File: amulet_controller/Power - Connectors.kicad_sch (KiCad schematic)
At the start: 4 parts, among them J1 XT60PW-F, J2 XT60PW-M, U6 SMBJ51CD-M3/H, U7 SMBJ51CD-M3/H

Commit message: filled in fields for bom, replaced inexisting components. Need to replace LEDs
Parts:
- J1: Manufacturer (none) -> AMASS; Manufacturer Part Number (none) -> XT60PW-F; Supplier 1 (none) -> Transfer Multisort Elektronik; Supplier Part Number 1 (none) -> XT60PW-F
- J2: Manufacturer (none) -> AMASS; Manufacturer Part Number (none) -> XT60PW-M; Supplier 1 (none) -> Transfer Multisort Elektronik; Supplier Part Number 1 (none) -> XT60PW-M
- U6, U7: Manufacturer (none) -> Vishay; Manufacturer Part Number (none) -> SMBJ51CD-M3/H; Supplier 1 (none) -> Digikey; Supplier Part Number 1 (none) -> SMBJ51CD-M3/HGICT-ND
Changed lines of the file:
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@@
     (pin "1")
     (instances
-      (project "bldc_controller"
+      (project "amulet_controller"
         (path "/0650c7a8-acba-429c-9f8e-eec0baf0bc1c/fede4c36-00cc-4d3d-b71c-5243ba232202/957e9462-5e63-4479-b30f-86013896ffc2"
           (reference "#PWR024") (unit 1)
@@
       (effects (font (size 1.27 1.27)) hide)
     )
-    (property "Datasheet" "~" (at 115.57 87.63 0)
+    (property "Datasheet" "https://www.tme.eu/Document/b13629717d44ae038681dba08d18c0b6/XT60PW-M.pdf" (at 115.57 87.63 0)
+      (effects (font (size 1.27 1.27)) hide)
+    )
+    (property "Description" "Socket; DC supply; XT60; male; PIN: 2; on PCBs; THT; yellow; 30A; 500V" (at 115.57 87.63 0)
+      (effects (font (size 1.27 1.27)) hide)
+    )
+    (property "Manufacturer" "AMASS" (at 115.57 87.63 0)
+      (effects (font (size 1.27 1.27)) hide)
+    )
+    (property "Manufacturer Part Number" "XT60PW-M" (at 115.57 87.63 0)
+      (effects (font (size 1.27 1.27)) hide)
+    )
+    (property "Supplier 1" "Transfer Multisort Elektronik" (at 115.57 87.63 0)
+      (effects (font (size 1.27 1.27)) hide)
+    )
+    (property "Supplier Part Number 1" "XT60PW-M" (at 115.57 87.63 0)
       (effects (font (size 1.27 1.27)) hide)
     )
@@
     (pin "2")
     (instances
-      (project "bldc_controller"
+      (project "amulet_controller"
         (path "/0650c7a8-acba-429c-9f8e-eec0baf0bc1c/fede4c36-00cc-4d3d-b71c-5243ba232202/957e9462-5e63-4479-b30f-86013896ffc2"
           (reference "J2") (unit 1)
@@
       (effects (font (size 1.27 1.27)) hide)
     )
+    (property "Description" "Surface-Mount TRANSZORB® Transient Voltage Suppressors" (at 135.89 77.47 0)
+      (effects (font (size 1.27 1.27)) hide)
+    )
+    (property "Manufacturer" "Vishay" (at 135.89 77.47 0)
+      (effects (font (size 1.27 1.27)) hide)
+    )
+    (property "Manufacturer Part Number" "SMBJ51CD-M3/H" (at 135.89 77.47 0)
+      (effects (font (size 1.27 1.27)) hide)
+    )
+    (property "Supplier 1" "Digikey" (at 135.89 77.47 0)
+      (effects (font (size 1.27 1.27)) hide)
+    )
+    (property "Supplier Part Number 1" "SMBJ51CD-M3/HGICT-ND" (at 135.89 77.47 0)
+      (effects (font (size 1.27 1.27)) hide)
+    )
     (pin "1")
     (pin "2")
     (instances
-      (project "bldc_controller"
+      (project "amulet_controller"
         (path "/0650c7a8-acba-429c-9f8e-eec0baf0bc1c/fede4c36-00cc-4d3d-b71c-5243ba232202/957e9462-5e63-4479-b30f-86013896ffc2"
           (reference "U6") (unit 1)
@@
       (effects (font (size 1.27 1.27)) hide)
     )
+    (property "Description" "Surface-Mount TRANSZORB® Transient Voltage Suppressors" (at 158.75 77.47 0)
+      (effects (font (size 1.27 1.27)) hide)
+    )
+    (property "Manufacturer" "Vishay" (at 158.75 77.47 0)
+      (effects (font (size 1.27 1.27)) hide)
+    )
+    (property "Manufacturer Part Number" "SMBJ51CD-M3/H" (at 158.75 77.47 0)
+      (effects (font (size 1.27 1.27)) hide)
+    )
+    (property "Supplier 1" "Digikey" (at 158.75 77.47 0)
+      (effects (font (size 1.27 1.27)) hide)
+    )
+    (property "Supplier Part Number 1" "SMBJ51CD-M3/HGICT-ND" (at 158.75 77.47 0)
+      (effects (font (size 1.27 1.27)) hide)
+    )
     (pin "1")
     (pin "2")
     (instances
-      (project "bldc_controller"
+      (project "amulet_controller"
         (path "/0650c7a8-acba-429c-9f8e-eec0baf0bc1c/fede4c36-00cc-4d3d-b71c-5243ba232202/957e9462-5e63-4479-b30f-86013896ffc2"
           (reference "U7") (unit 1)
@@
       (effects (font (size 1.27 1.27)) hide)
     )
-    (property "Datasheet" "~" (at 115.57 78.74 0)
+    (property "Datasheet" "https://www.tme.eu/Document/1191bc2fa3aee3c446e5a895fd8f7983/XT60PW-F.pdf" (at 115.57 78.74 0)
+      (effects (font (size 1.27 1.27)) hide)
+    )
+    (property "Description" "Socket; DC supply; XT60; female; PIN: 2; on PCBs; THT; yellow; 30A" (at 115.57 78.74 0)
+      (effects (font (size 1.27 1.27)) hide)
+    )
+    (property "Manufacturer" "AMASS" (at 115.57 78.74 0)
+      (effects (font (size 1.27 1.27)) hide)
+    )
+    (property "Manufacturer Part Number" "XT60PW-F" (at 115.57 78.74 0)
+      (effects (font (size 1.27 1.27)) hide)
+    )
+    (property "Supplier 1" "Transfer Multisort Elektronik" (at 115.57 78.74 0)
+      (effects (font (size 1.27 1.27)) hide)
+    )
+    (property "Supplier Part Number 1" "XT60PW-F" (at 115.57 78.74 0)
       (effects (font (size 1.27 1.27)) hide)
     )
@@
     (pin "2")
     (instances
-      (project "bldc_controller"
+      (project "amulet_controller"
         (path "/0650c7a8-acba-429c-9f8e-eec0baf0bc1c/fede4c36-00cc-4d3d-b71c-5243ba232202/957e9462-5e63-4479-b30f-86013896ffc2"
           (reference "J1") (unit 1)

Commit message: added test points
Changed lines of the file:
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@@
     (effects (font (face "Arial") (size 1.27 1.27) (color 0 0 0 1)) (justify left top))
   )
-  (text_box "Power Connectors, TVS diodes and electrolytic bulk capacitors"
+  (text_box "Power Connectors, TVS Diodes"
     (at 80.01 124.46 0) (size 134.62 9.525)
     (stroke (width -0.0001) (type default))

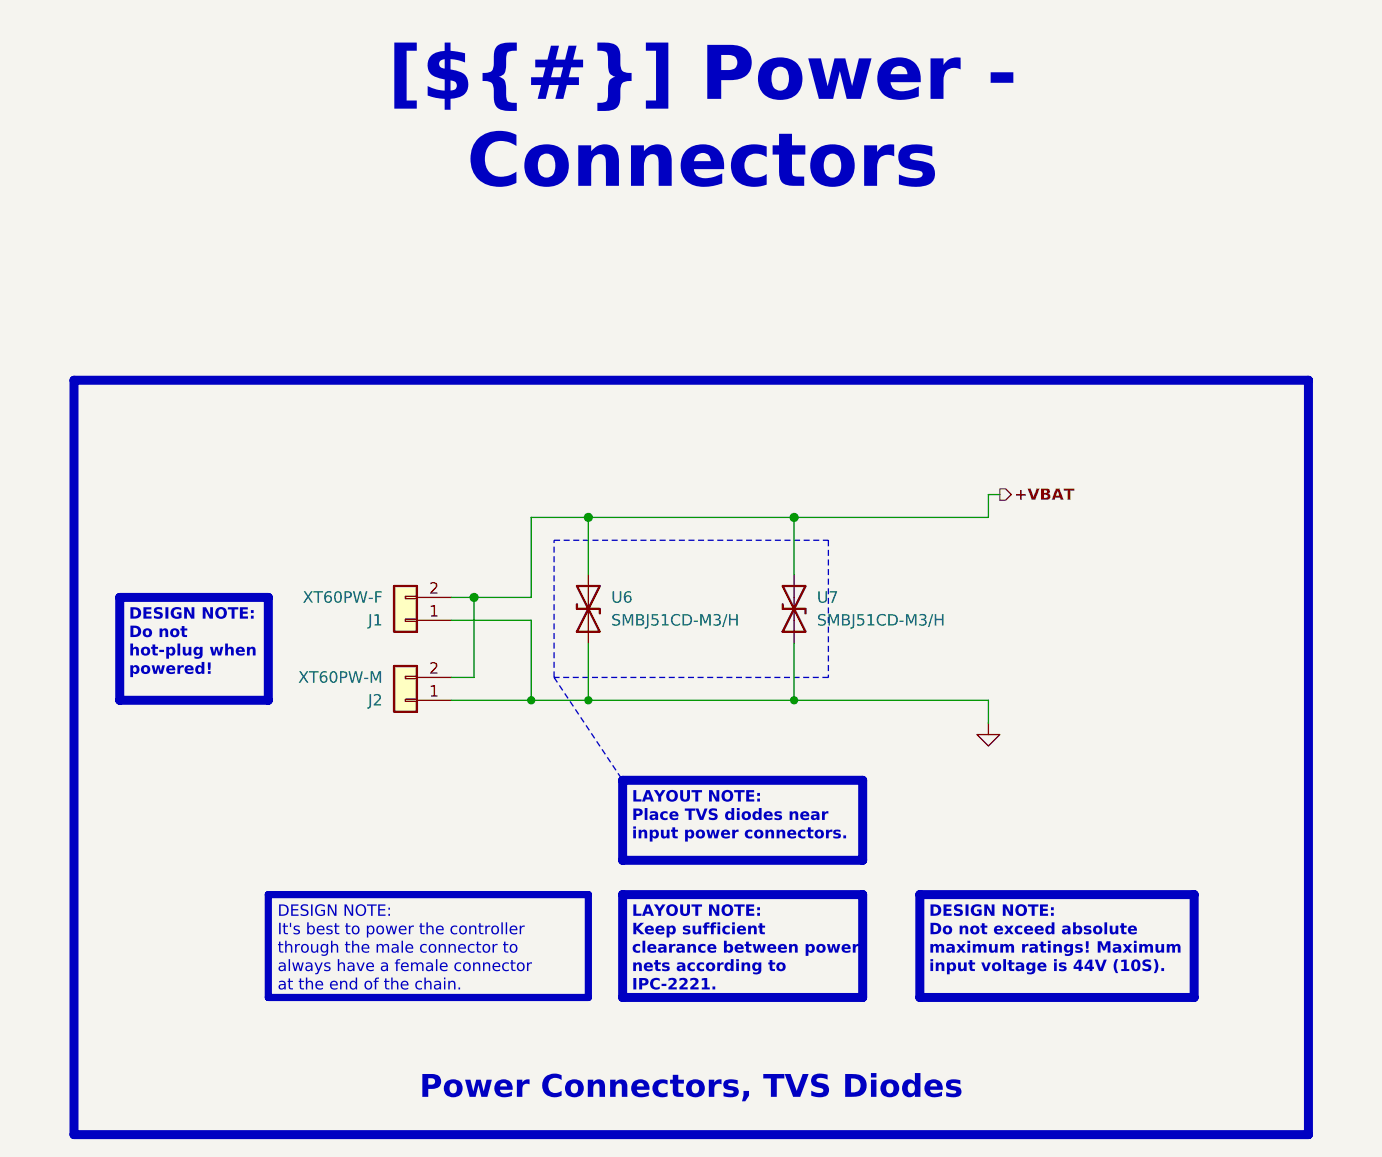
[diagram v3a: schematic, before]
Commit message: corrected pcb according to reviews on reddit
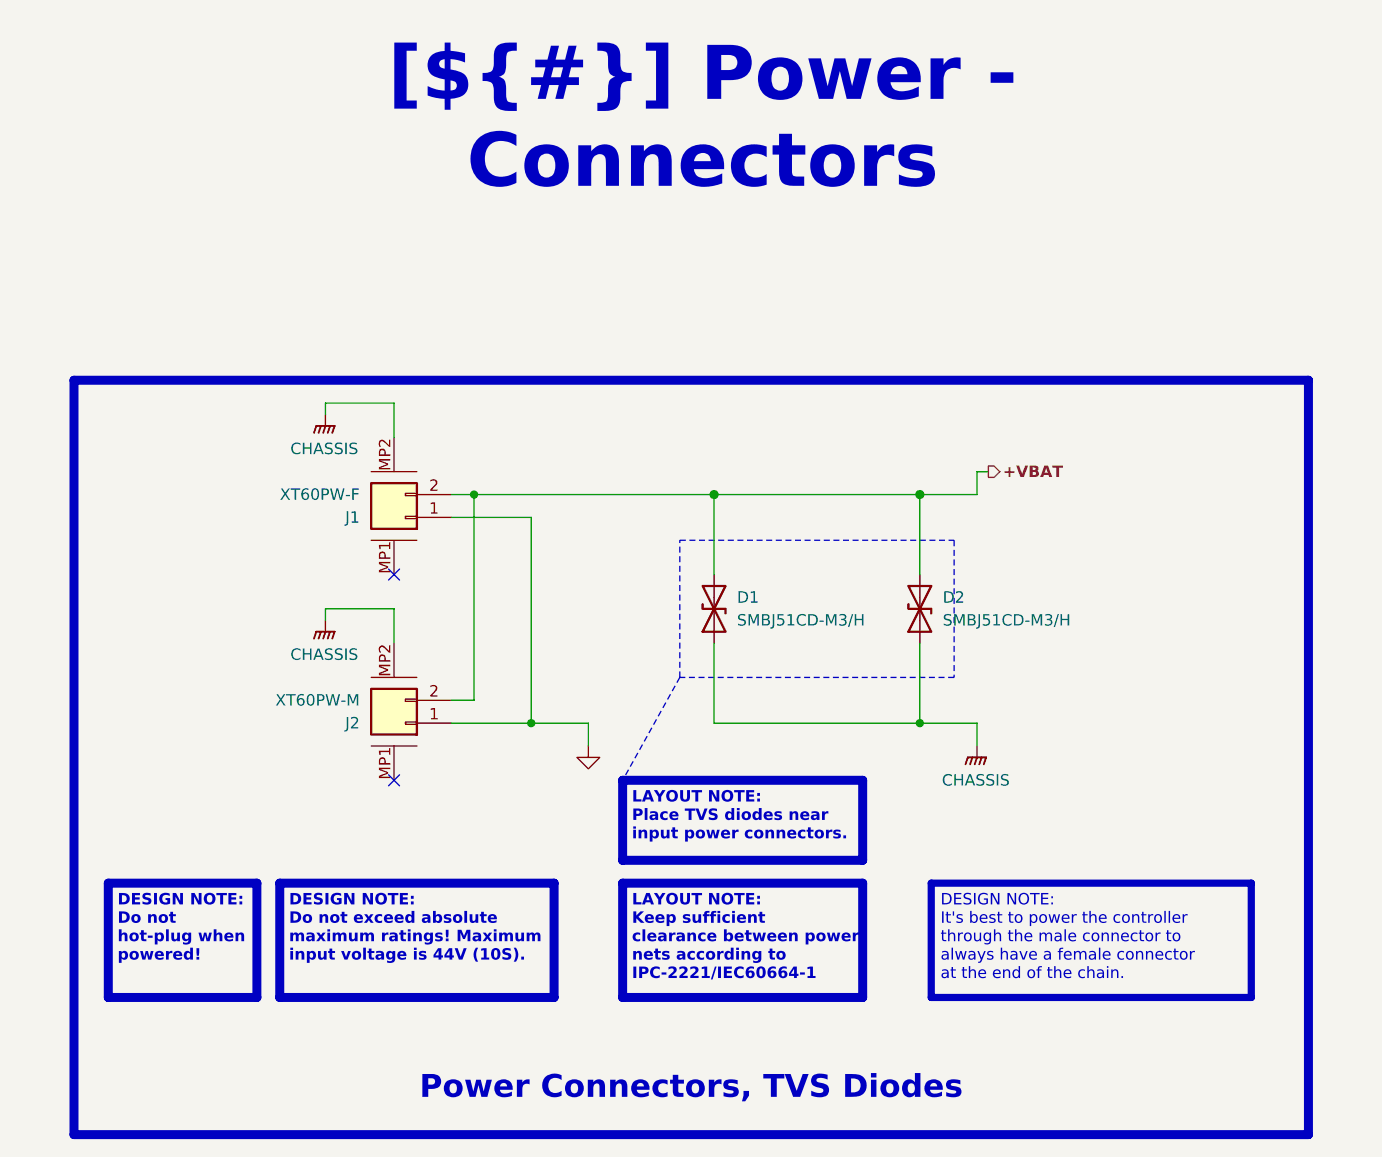
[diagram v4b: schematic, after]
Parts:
- J1, J2: symbol Connector_Generic:Conn_01x02 -> 0_connectors:Conn_01x02_Mounting
- renumbered U6 to D1, U7 to D2
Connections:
- net GND: no longer D1.1 (A1), D2.1 (A1)
- new net CHASSIS: D1.1 (A1), D2.1 (A1), J1.MP2, J2.MP2
- no-connect marks 0 -> 2
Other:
- moved on the sheet: D1, D2
